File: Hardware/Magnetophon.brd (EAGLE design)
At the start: 105 x 19 mm, 22 parts, among them U2 TL072_

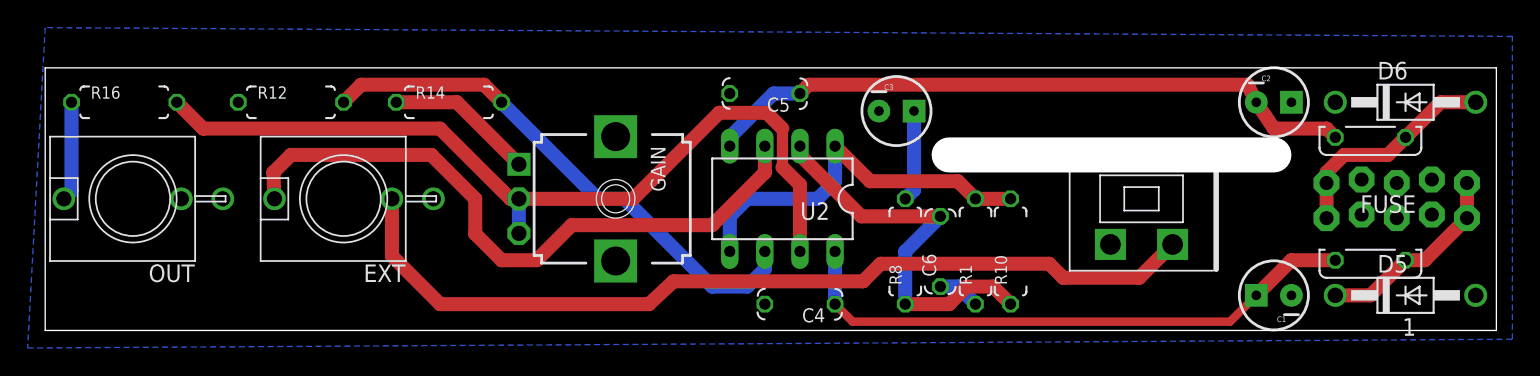
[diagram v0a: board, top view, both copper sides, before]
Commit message: add 10n cap and reroute
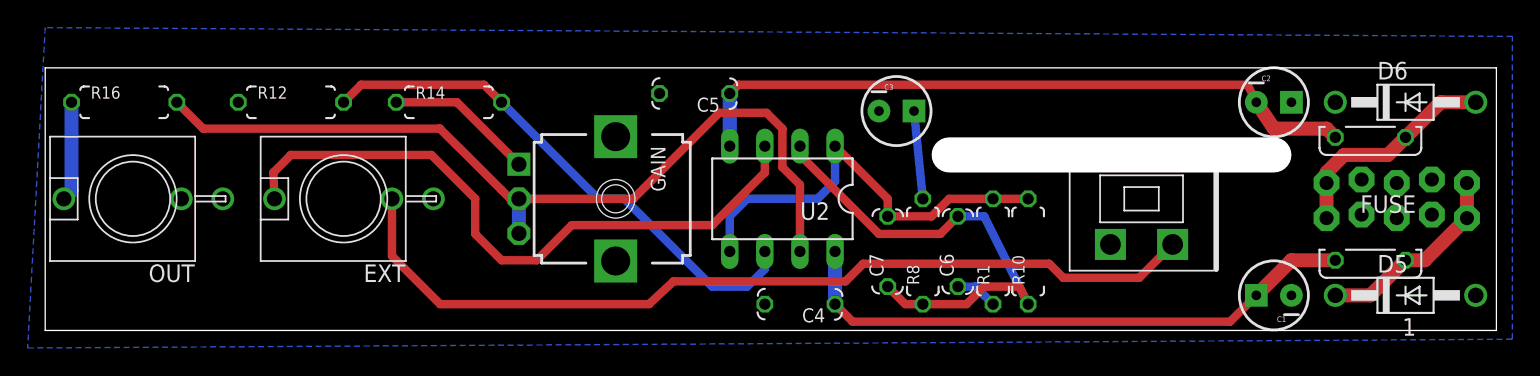
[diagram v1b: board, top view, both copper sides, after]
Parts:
- added C7: 10nf, TomW:C050-024X044
- moved C5 5.08 mm to (47.0, 17.1)
- moved C6 1.27 mm to (66.0, 5.71)
- moved R10 1.27 mm to (71.1, 5.71)
- moved R8 1.27 mm to (63.5, 5.71)
- moved R1 1.27 mm to (68.6, 5.71)
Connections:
- net N$3: now also C7.1
- net N$4: now also C7.2
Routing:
- net N$3: track 28.7 -> 36.0 mm
- net N$4: track 28.0 -> 31.1 mm
- net -12V: track 48.1 -> 50.0 mm

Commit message: improved layout and curves
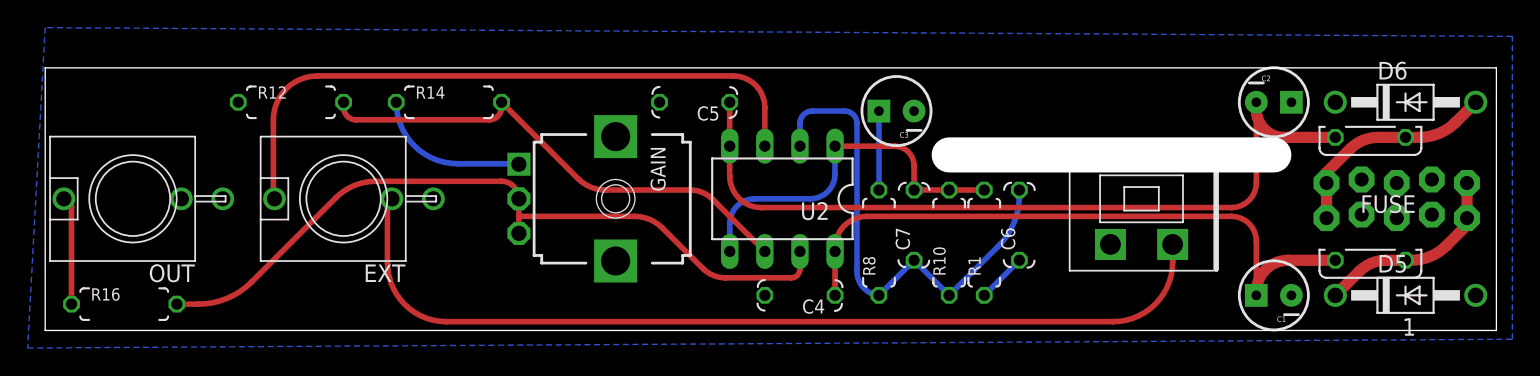
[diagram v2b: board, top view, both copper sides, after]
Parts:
- moved R16 14.6 mm to (5.71, 1.91)
- moved R10 5.75 mm to (65.4, 6.35)
- moved C6 4.84 mm to (70.5, 7.62)
- moved R8 3.24 mm to (60.3, 6.35)
- moved C7 2.69 mm to (62.9, 7.62)
- moved R1 0.90 mm to (67.9, 6.35)
- moved C4 0.64 mm to (54.6, 2.54)
- moved C5 0.63 mm to (47.0, 16.5)
- turned C3 to 180 degrees
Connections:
- net N$1 renamed FROMHEAD
- net N$2 renamed TOAMP
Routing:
- net -12V: track 50.0 -> 57.5 mm
- net N$8: track 61.7 -> 54.2 mm
- net N$4: track 31.1 -> 26.3 mm
- net +12V: track 42.4 -> 46.2 mm
- net N$6: track 38.9 -> 36.1 mm
- net FROMHEAD: track 64.7 -> 66.5 mm
- net TOAMP: track 47.2 -> 46.4 mm
- net N$7: track 6.38 -> 5.71 mm
- net N$10: track 7.21 -> 7.85 mm
- net N$3: track 36.0 -> 36.5 mm
- net N$9: track 3.07 -> 3.59 mm
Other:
- board text added: "Magnetophon Music Thing Modular Designed in Herne Hill, London By Tom Whitwell April 2016 PCB Prototype 2 CC-BY-SA"
- board text removed: "Magnetophon Music Thing Modular Designed in Herne Hill, London By Tom Whitwell October 2015 PCB Prototype 1 CC-BY-SA"

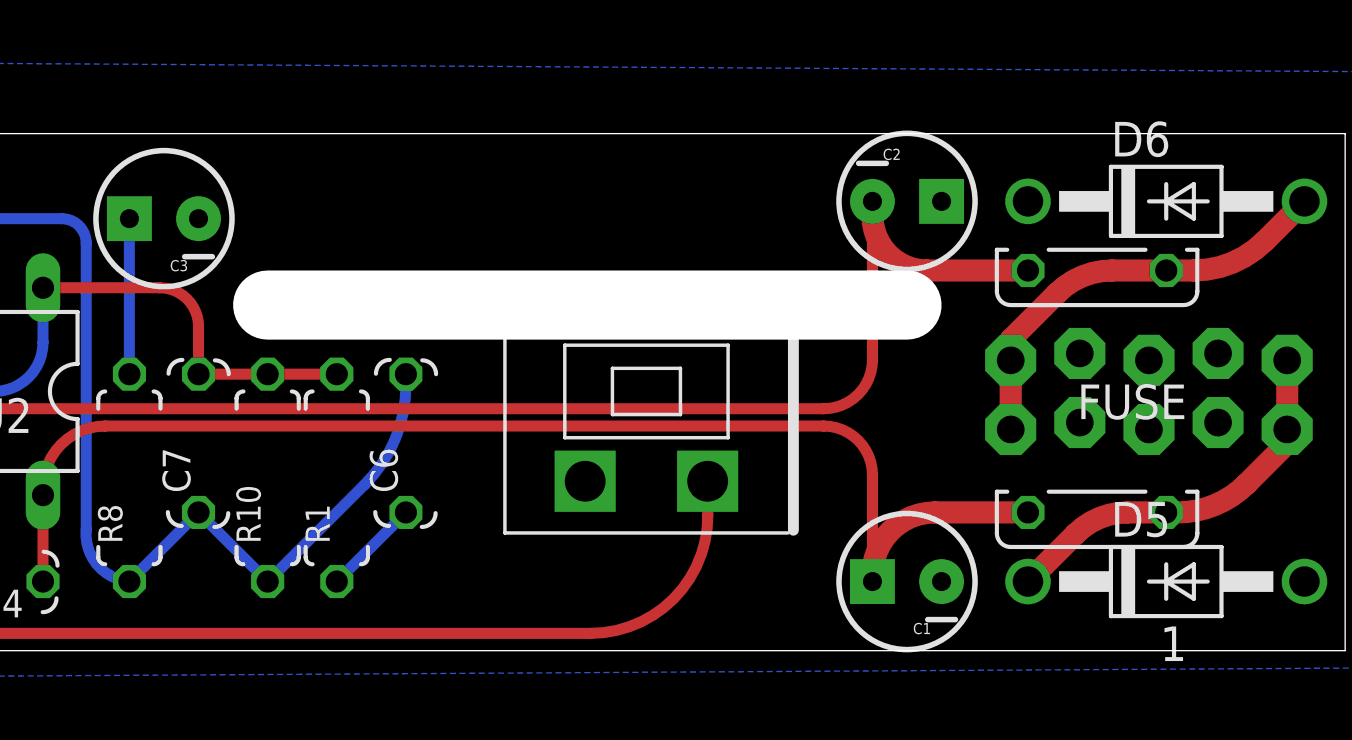
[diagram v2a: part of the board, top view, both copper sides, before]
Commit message: Small board tweaks, fixes #1, fixes #2, fixes #3, fixes #4
#1 and #2 fixed by improved layout, #3 and #4 with tweaks here
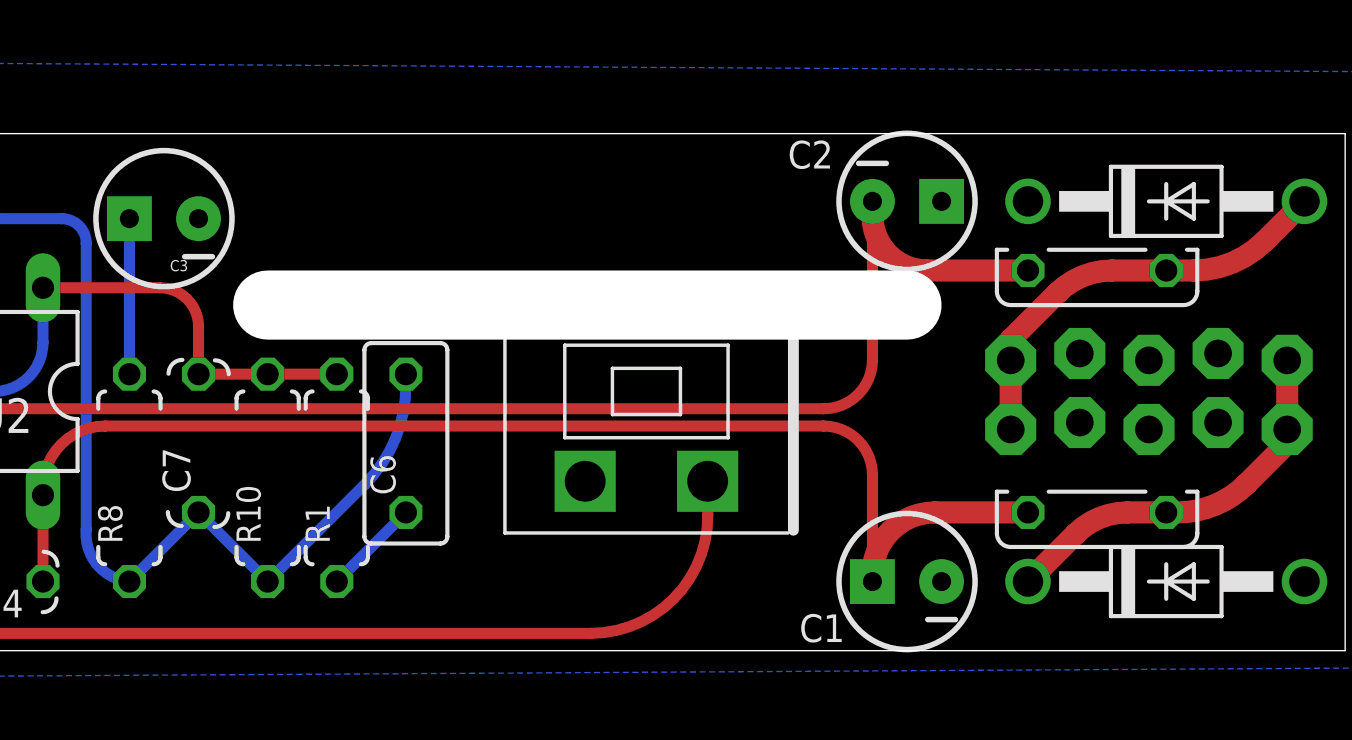
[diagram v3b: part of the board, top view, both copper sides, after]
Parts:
- C6: device TomW:C050-024X044 -> rcl:C050-030X075
- C7: value 10nf -> DNP
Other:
- board text added: "Magnetophon Music Thing Modular Designed in Herne Hill, London By Tom Whitwell May 2016 PCB Rev 1 CC-BY-SA"
- board text removed: "Magnetophon Music Thing Modular Designed in Herne Hill, London By Tom Whitwell April 2016 PCB Prototype 2 CC-BY-SA"
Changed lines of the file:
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@@
 <?xml version="1.0" encoding="utf-8"?>
 <!DOCTYPE eagle SYSTEM "eagle.dtd">
-<eagle version="7.4.0">
+<eagle version="7.2.0">
 <drawing>
 <settings>
@@
 <grid distance="25" unitdist="mil" unit="mil" style="lines" multiple="1" display="yes" altdistance="12.5" altunitdist="mil" altunit="mil"/>
 <layers>
-<layer number="1" name="Top" color="4" fill="1" visible="yes" active="yes"/>
+<layer number="1" name="Top" color="4" fill="1" visible="no" active="yes"/>
 <layer number="2" name="Route2" color="1" fill="3" visible="no" active="yes"/>
 <layer number="3" name="Route3" color="4" fill="3" visible="no" active="no"/>
@@
 <layer number="15" name="Route15" color="4" fill="6" visible="no" active="yes"/>
 <layer number="16" name="Bottom" color="1" fill="1" visible="yes" active="yes"/>
-<layer number="17" name="Pads" color="2" fill="1" visible="yes" active="yes"/>
-<layer number="18" name="Vias" color="2" fill="1" visible="yes" active="yes"/>
-<layer number="19" name="Unrouted" color="6" fill="1" visible="yes" active="yes"/>
+<layer number="17" name="Pads" color="2" fill="1" visible="no" active="yes"/>
+<layer number="18" name="Vias" color="2" fill="1" visible="no" active="yes"/>
+<layer number="19" name="Unrouted" color="6" fill="1" visible="no" active="yes"/>
 <layer number="20" name="Dimension" color="15" fill="1" visible="yes" active="yes"/>
 <layer number="21" name="tPlace" color="7" fill="1" visible="no" active="yes"/>
-<layer number="22" name="bPlace" color="7" fill="1" visible="no" active="yes"/>
+<layer number="22" name="bPlace" color="7" fill="1" visible="yes" active="yes"/>
 <layer number="23" name="tOrigins" color="15" fill="1" visible="no" active="yes"/>
-<layer number="24" name="bOrigins" color="15" fill="1" visible="no" active="yes"/>
+<layer number="24" name="bOrigins" color="15" fill="1" visible="yes" active="yes"/>
 <layer number="25" name="tNames" color="7" fill="1" visible="no" active="yes"/>
 <layer number="26" name="bNames" color="7" fill="1" visible="no" active="yes"/>
@@
 <layer number="28" name="bValues" color="7" fill="1" visible="no" active="yes"/>
 <layer number="29" name="tStop" color="7" fill="3" visible="no" active="yes"/>
-<layer number="30" name="bStop" color="7" fill="6" visible="no" active="yes"/>
+<layer number="30" name="bStop" color="7" fill="6" visible="yes" active="yes"/>
 <layer number="31" name="tCream" color="7" fill="4" visible="no" active="yes"/>
 <layer number="32" name="bCream" color="7" fill="5" visible="no" active="yes"/>
@@
 Music Thing Modular
 Designed in Herne Hill, London
-By Tom Whitwell April  2016
-PCB Prototype 2 CC-BY-SA</text>
+By Tom Whitwell May  2016
+PCB Rev 1 CC-BY-SA</text>
 <text x="32.512" y="11.557" size="0.762" layer="30" font="vector" ratio="12" distance="40" rot="MR0">Inspired by: Laurie Anderson, Nam June Paik,
 Brian Eno, Stockhausen, Yoko Ono, Steve Reich,
@@
 <element name="R10" library="MusicThingModular" package="7MM_RESISTOR" value="200k" x="65.405" y="6.35" rot="R90"/>
 <element name="R12" library="MusicThingModular" package="7MM_RESISTOR" value="2.2k" x="17.78" y="16.51"/>
-<element name="C1" library="SparkFun-Passives" package="CPOL-RADIAL-10UF-25V" value="10uf" x="88.9" y="2.54" rot="R180"/>
+<element name="C1" library="SparkFun-Passives" package="CPOL-RADIAL-10UF-25V" value="10uf" x="88.9" y="2.54" smashed="yes" rot="R180">
+<attribute name="NAME" x="86.614" y="1.3335" size="1.016" layer="25" rot="R180"/>
+<attribute name="VALUE" x="90.805" y="6.223" size="1.016" layer="27" rot="R180"/>
+</element>
 <element name="C4" library="TomW" package="C050-024X044" value="100n" x="54.61" y="2.54" rot="R180"/>
 <element name="C5" library="TomW" package="C050-024X044" value="100n" x="46.99" y="16.51" rot="R180"/>
-<element name="C2" library="SparkFun-Passives" package="CPOL-RADIAL-10UF-25V" value="10uf" x="88.9" y="16.51"/>
-<element name="D5" library="diode" package="DO41-10" value="1N4001" x="98.425" y="2.54"/>
-<element name="D6" library="diode" package="DO41-10" value="1N4001" x="98.425" y="16.51"/>
-<element name="1" library="TomW" package="C050H075X075" value="FUSE" x="95.885" y="5.08" rot="R180"/>
-<element name="FUSE" library="TomW" package="C050H075X075" value="FUSE" x="95.885" y="13.97" rot="R180"/>
+<element name="C2" library="SparkFun-Passives" package="CPOL-RADIAL-10UF-25V" value="10uf" x="88.9" y="16.51" smashed="yes">
+<attribute name="NAME" x="84.5185" y="17.7165" size="1.016" layer="25"/>
+<attribute name="VALUE" x="87.63" y="12.827" size="1.016" layer="27"/>
+</element>
+<element name="D5" library="diode" package="DO41-10" value="1N4001" x="98.425" y="2.54" smashed="yes"/>
+<element name="D6" library="diode" package="DO41-10" value="1N4001" x="98.425" y="16.51" smashed="yes"/>
+<element name="1" library="TomW" package="C050H075X075" value="FUSE" x="95.885" y="5.08" smashed="yes" rot="R180">
+<attribute name="VALUE" x="97.79" y="5.3975" size="0.9144" layer="27" ratio="10" rot="R180"/>
+</element>
+<element name="FUSE" library="TomW" package="C050H075X075" value="FUSE" x="95.885" y="13.97" smashed="yes" rot="R180">
+<attribute name="VALUE" x="97.79" y="14.2875" size="0.9144" layer="27" ratio="10" rot="R180"/>
+</element>
 <element name="U$1" library="MusicThingModular" package="MONO_CASSETTE_HEAD" value="MONO_CASSETTE_HEAD" x="79.3242" y="9.525" rot="R180"/>
-<element name="C3" library="SparkFun-Passives" package="CPOL-RADIAL-10UF-25V" value="47uf" x="61.595" y="15.875" rot="R180"/>
-<element name="C6" library="TomW" package="C050-024X044" value="15nf" x="70.485" y="7.62" rot="R90"/>
+<element name="C3" library="SparkFun-Passives" package="CPOL-RADIAL-10UF-25V" value="47uf" x="61.595" y="15.875" smashed="yes" rot="R180">
+<attribute name="NAME" x="62.484" y="14.351" size="0.4064" layer="25" rot="R180"/>
+<attribute name="VALUE" x="67.945" y="18.288" size="1.016" layer="27" rot="R180"/>
+</element>
+<element name="C6" library="rcl" package="C050-030X075" value="15nf" x="70.485" y="7.62" rot="R90"/>
 <element name="R1" library="MusicThingModular" package="7MM_RESISTOR" value="3.6k" x="67.945" y="6.35" rot="R90"/>
 <element name="EXT" library="MusicThingModular" package="WQP-PJ301M-12_JACK" value="THONKICONNNEW" x="21.59" y="9.525" rot="R90"/>
@@
 <element name="U2" library="MusicThingModular" package="DIL08" value="TL072_" x="53.34" y="9.525" rot="R180"/>
 <element name="U$2" library="MusicThingModular" package="EURO_PWR_HEADER_LOCK" value="EURO_POWER_LOCK" x="97.79" y="9.525" rot="MR180"/>
-<element name="C7" library="TomW" package="C050-024X044" value="10nf" x="62.865" y="7.62" rot="R90"/>
+<element name="C7" library="TomW" package="C050-024X044" value="DNP" x="62.865" y="7.62" rot="R90"/>
 </elements>
 <signals>
